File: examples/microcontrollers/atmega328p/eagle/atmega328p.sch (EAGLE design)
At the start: 7 parts, among them U1 ATMEGA328P_TQFP, Y1 8MHz

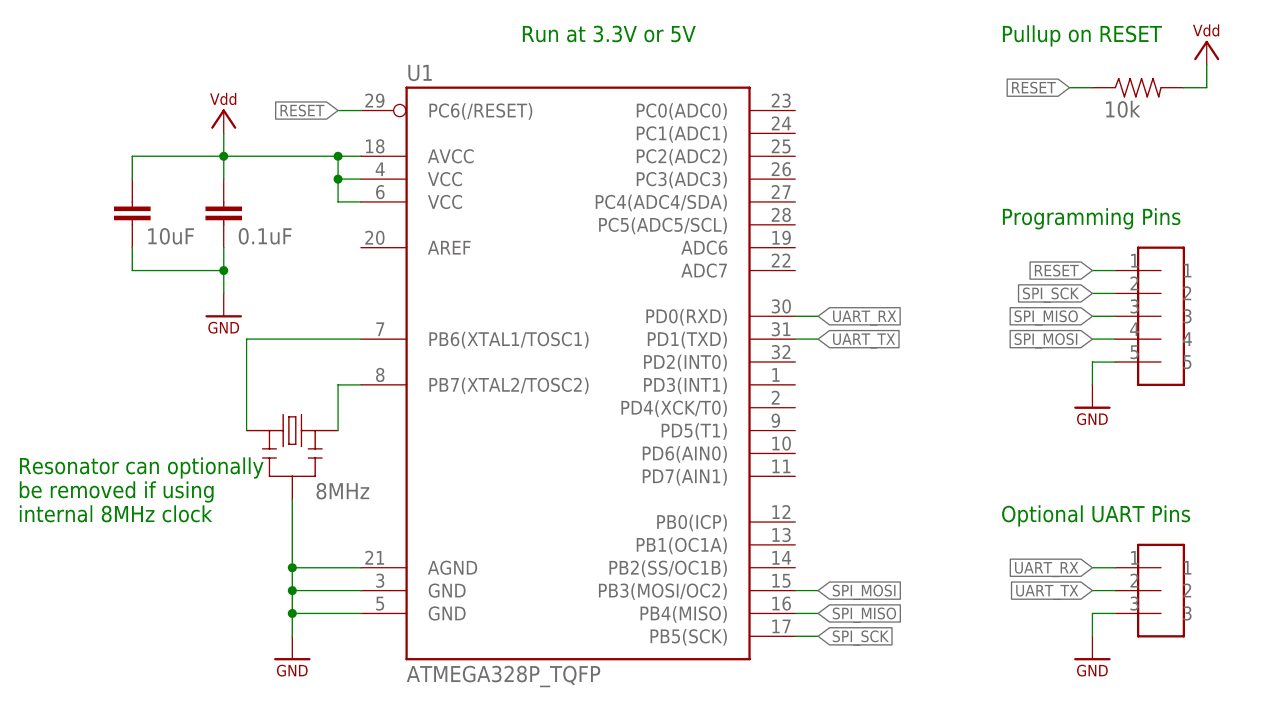
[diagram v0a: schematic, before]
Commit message: marquee template; schematic images
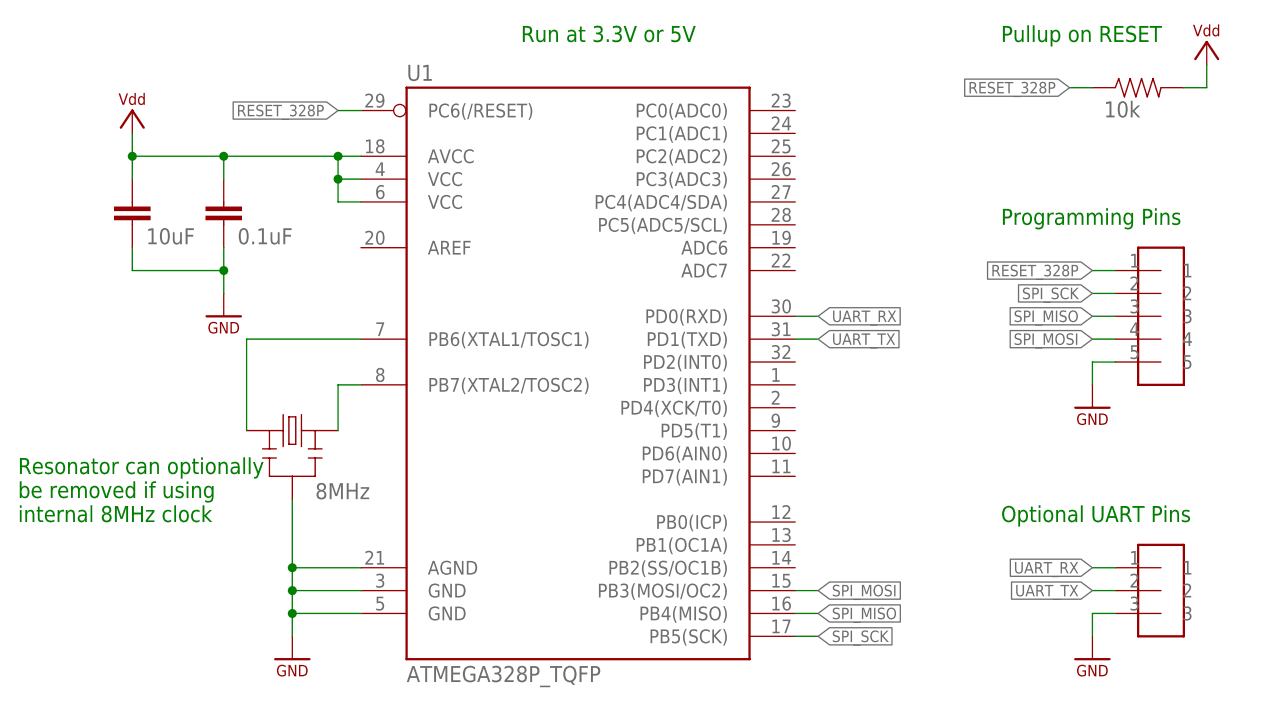
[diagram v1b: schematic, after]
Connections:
- net RESET renamed RESET_328P
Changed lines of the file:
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@@
 <attribute name="VALUE" x="45.72" y="2.54" size="1.778" layer="96"/>
 </instance>
-<instance part="P+1" gate="G$1" x="25.4" y="66.04" smashed="yes"/>
+<instance part="P+1" gate="G$1" x="15.24" y="66.04" smashed="yes"/>
 <instance part="GND1" gate="1" x="33.02" y="5.08" smashed="yes"/>
 <instance part="Y1" gate="G$1" x="33.02" y="30.48" smashed="yes">
@@
 </busses>
 <nets>
-<net name="RESET" class="0">
-<segment>
-<pinref part="U1" gate="U$1" pin="PC6(/RESET)"/>
-<wire x1="40.64" y1="66.04" x2="38.1" y2="66.04" width="0.1524" layer="91"/>
-<label x="38.1" y="66.04" size="1.27" layer="95" rot="R180" xref="yes"/>
-</segment>
-<segment>
-<pinref part="R1" gate="G$1" pin="1"/>
-<wire x1="121.92" y1="68.58" x2="119.38" y2="68.58" width="0.1524" layer="91"/>
-<label x="119.38" y="68.58" size="1.27" layer="95" rot="R180" xref="yes"/>
-</segment>
-<segment>
-<pinref part="U$2" gate="G$1" pin="1"/>
-<wire x1="124.46" y1="48.26" x2="121.92" y2="48.26" width="0.1524" layer="91"/>
-<label x="121.92" y="48.26" size="1.27" layer="95" rot="R180" xref="yes"/>
-</segment>
-</net>
 <net name="VDD" class="0">
 <segment>
@@
 <wire x1="38.1" y1="60.96" x2="25.4" y2="60.96" width="0.1524" layer="91"/>
 <pinref part="P+1" gate="G$1" pin="VDD"/>
-<wire x1="25.4" y1="60.96" x2="25.4" y2="63.5" width="0.1524" layer="91"/>
 <pinref part="C1" gate="G$1" pin="1"/>
 <wire x1="25.4" y1="58.42" x2="25.4" y2="60.96" width="0.1524" layer="91"/>
@@
 <pinref part="C2" gate="G$1" pin="1"/>
 <wire x1="15.24" y1="60.96" x2="15.24" y2="58.42" width="0.1524" layer="91"/>
+<wire x1="15.24" y1="63.5" x2="15.24" y2="60.96" width="0.1524" layer="91"/>
+<junction x="15.24" y="60.96"/>
 </segment>
 </net>
@@
 </segment>
 </net>
+<net name="RESET_328P" class="0">
+<segment>
+<pinref part="U1" gate="U$1" pin="PC6(/RESET)"/>
+<wire x1="40.64" y1="66.04" x2="38.1" y2="66.04" width="0.1524" layer="91"/>
+<label x="38.1" y="66.04" size="1.27" layer="95" rot="R180" xref="yes"/>
+</segment>
+<segment>
+<pinref part="R1" gate="G$1" pin="1"/>
+<wire x1="121.92" y1="68.58" x2="119.38" y2="68.58" width="0.1524" layer="91"/>
+<label x="119.38" y="68.58" size="1.27" layer="95" rot="R180" xref="yes"/>
+</segment>
+<segment>
+<pinref part="U$2" gate="G$1" pin="1"/>
+<wire x1="124.46" y1="48.26" x2="121.92" y2="48.26" width="0.1524" layer="91"/>
+<label x="121.92" y="48.26" size="1.27" layer="95" rot="R180" xref="yes"/>
+</segment>
+</net>
